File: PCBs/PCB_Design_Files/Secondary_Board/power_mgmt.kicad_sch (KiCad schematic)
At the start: 19 parts, among them Q3 MMBT3904, Q4 MMBT3904, U5 TPS61023DRLR, U6 TLV9101IDCKR

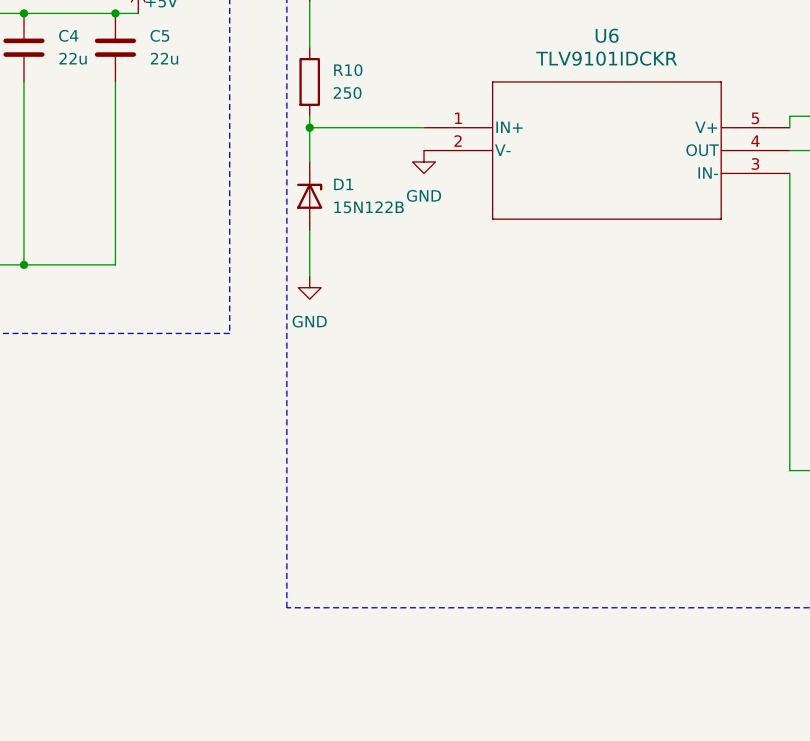
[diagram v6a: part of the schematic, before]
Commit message: change zener
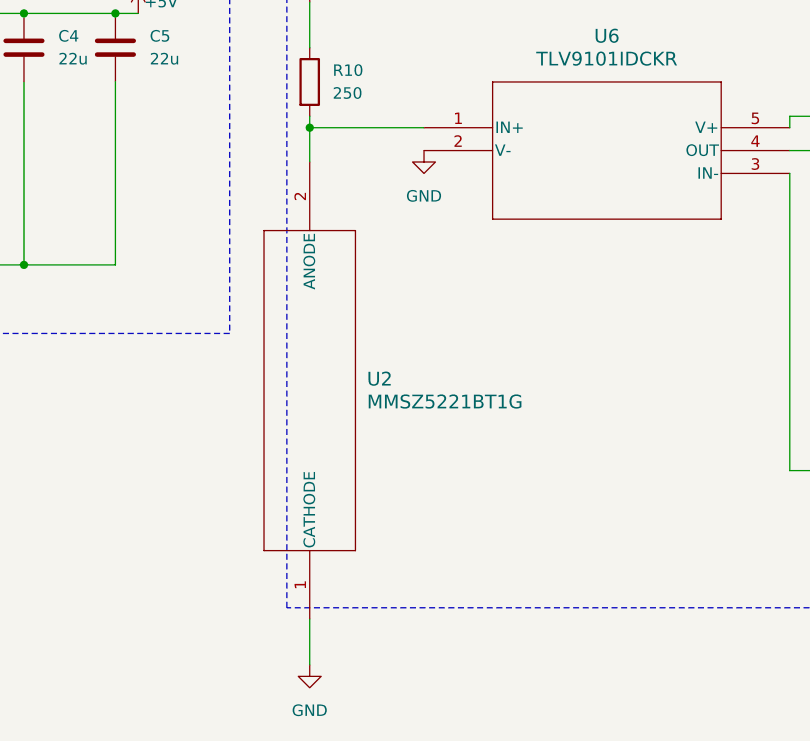
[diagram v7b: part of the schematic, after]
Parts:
- removed D1: 15N122B, Diode_THT:D_DO-35_SOD27_P7.62mm_Horizontal, symbol Device:D_Zener
- added U2: MMSZ5221BT1G, Project Footprints:SOD-123_ONS, symbol Project_Symbols:MMSZ5221BT1G
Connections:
- net GND: now also U2.1 (CATHODE)
- net at R10.2, U6.1 (IN+): now also U2.2 (ANODE)
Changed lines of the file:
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@@
 	(wire
 		(pts
-			(xy 144.78 106.68) (xy 144.78 111.76)
+			(xy 144.78 149.86) (xy 144.78 154.94)
 		)
 		(stroke
@@
 	(symbol
 		(lib_id "power:GND")
-		(at 144.78 111.76 0)
+		(at 144.78 154.94 0)
 		(unit 1)
 		(exclude_from_sim no)
@@
 		(fields_autoplaced yes)
 		(property "Reference" "#PWR0103"
-			(at 144.78 118.11 0)
+			(at 144.78 161.29 0)
 			(effects
 				(font
@@
 		)
 		(property "Value" "GND"
-			(at 144.78 116.84 0)
+			(at 144.78 160.02 0)
 			(effects
 				(font
@@
 		)
 		(property "Footprint" ""
-			(at 144.78 111.76 0)
+			(at 144.78 154.94 0)
 			(effects
 				(font
@@
 		)
 		(property "Datasheet" ""
-			(at 144.78 111.76 0)
+			(at 144.78 154.94 0)
 			(effects
 				(font
@@
 		)
 		(property "Description" "Power symbol creates a global label with name \"GND\" , ground"
-			(at 144.78 111.76 0)
+			(at 144.78 154.94 0)
 			(effects
 				(font
@@
 	)
 	(symbol
+		(lib_id "Project_Symbols:MMSZ5221BT1G")
+		(at 144.78 149.86 90)
+		(unit 1)
+		(exclude_from_sim no)
+		(in_bom yes)
+		(on_board yes)
+		(dnp no)
+		(fields_autoplaced yes)
+		(property "Reference" "U2"
+			(at 151.13 123.1899 90)
+			(effects
+				(font
+					(size 1.524 1.524)
+				)
+				(justify right)
+			)
+		)
+		(property "Value" "MMSZ5221BT1G"
+			(at 151.13 125.7299 90)
+			(effects
+				(font
+					(size 1.524 1.524)
+				)
+				(justify right)
+			)
+		)
+		(property "Footprint" "Project Footprints:SOD-123_ONS"
+			(at 144.78 149.86 0)
+			(effects
+				(font
+					(size 1.27 1.27)
+					(italic yes)
+				)
+				(hide yes)
+			)
+		)
+		(property "Datasheet" "MMSZ5221BT1G"
+			(at 144.78 149.86 0)
+			(effects
+				(font
+					(size 1.27 1.27)
+					(italic yes)
+				)
+				(hide yes)
+			)
+		)
+		(property "Description" ""
+			(at 144.78 149.86 0)
+			(effects
+				(font
+					(size 1.27 1.27)
+				)
+				(hide yes)
+			)
+		)
+		(pin "1"
+		)
+		(pin "2"
+		)
+		(instances
+			(project ""
+				(path "/2f5986e4-77b2-4f5d-ab91-80ba6228eb8b/3db8306c-5846-4ae5-ba17-fe529edf9e71"
+					(reference "U2")
+					(unit 1)
+				)
+			)
+		)
+	)
+	(symbol
 		(lib_id "power:VCC")
 		(at 27.94 26.67 0)
@@
 					(unit 1)
 				)
-			)
-		)
-	)
-	(symbol
-		(lib_id "Device:D_Zener")
-		(at 144.78 102.87 270)
-		(unit 1)
-		(exclude_from_sim no)
-		(in_bom yes)
-		(on_board yes)
-		(dnp no)
-		(fields_autoplaced yes)
-		(property "Reference" "D1"
-			(at 147.32 101.5999 90)
-			(effects
-				(font
-					(size 1.27 1.27)
-				)
-				(justify left)
-			)
-		)
-		(property "Value" "15N122B"
-			(at 147.32 104.1399 90)
-			(effects
-				(font
-					(size 1.27 1.27)
-				)
-				(justify left)
-			)
-		)
-		(property "Footprint" "Diode_THT:D_DO-35_SOD27_P7.62mm_Horizontal"
-			(at 144.78 102.87 0)
-			(effects
-				(font
-					(size 1.27 1.27)
-				)
-				(hide yes)
-			)
-		)
-		(property "Datasheet" "~"
-			(at 144.78 102.87 0)
-			(effects
-				(font
-					(size 1.27 1.27)
-				)
-				(hide yes)
-			)
-		)
-		(property "Description" "Zener diode"
-			(at 144.78 102.87 0)
-			(effects
-				(font
-					(size 1.27 1.27)
-				)
-				(hide yes)
-			)
-		)
-		(pin "1"
-		)
-		(pin "2"
-		)
-		(instances
-			(project "Secondary_Board"
-				(path "/2f5986e4-77b2-4f5d-ab91-80ba6228eb8b/3db8306c-5846-4ae5-ba17-fe529edf9e71"
-					(reference "D1")
-					(unit 1)
-				)
-			)
-			(project "power_mgmt"
-				(path "/c7abdc65-9966-45f8-babc-768b62a50249"
-					(reference "D1")
-					(unit 1)
-				)

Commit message: secondary board connectors
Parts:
- removed BT1: Battery, Connector_JST:JST_PH_S2B-PH-K_1x02_P2.00mm_Horizontal, symbol Device:Battery
- added BT2: Battery_Cell, Project Footprints:bat_pads, symbol Device:Battery_Cell
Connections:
- net +3.7V: now also BT2.1 (+)
- net GND: now also BT2.2 (-)
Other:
- moved on the sheet: C6, C7, Q3, Q4, R10, R11, R12, R13, U2, U6
